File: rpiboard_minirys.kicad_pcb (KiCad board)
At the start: 4 copper layers, 65 x 56 mm, 128 parts, among them IC1 LM51231QRGRRQ1, IC2 TPS564242DRLR, IC3 L6470H, IC4 L6470H, IC5 74AUP2G00DC,125, IC6 MAX11613EUA+T, J1 RPi_GPIO, J10 ToF1_Sensor, J11 ToF2_Sensor, J12 ToF3_Sensor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

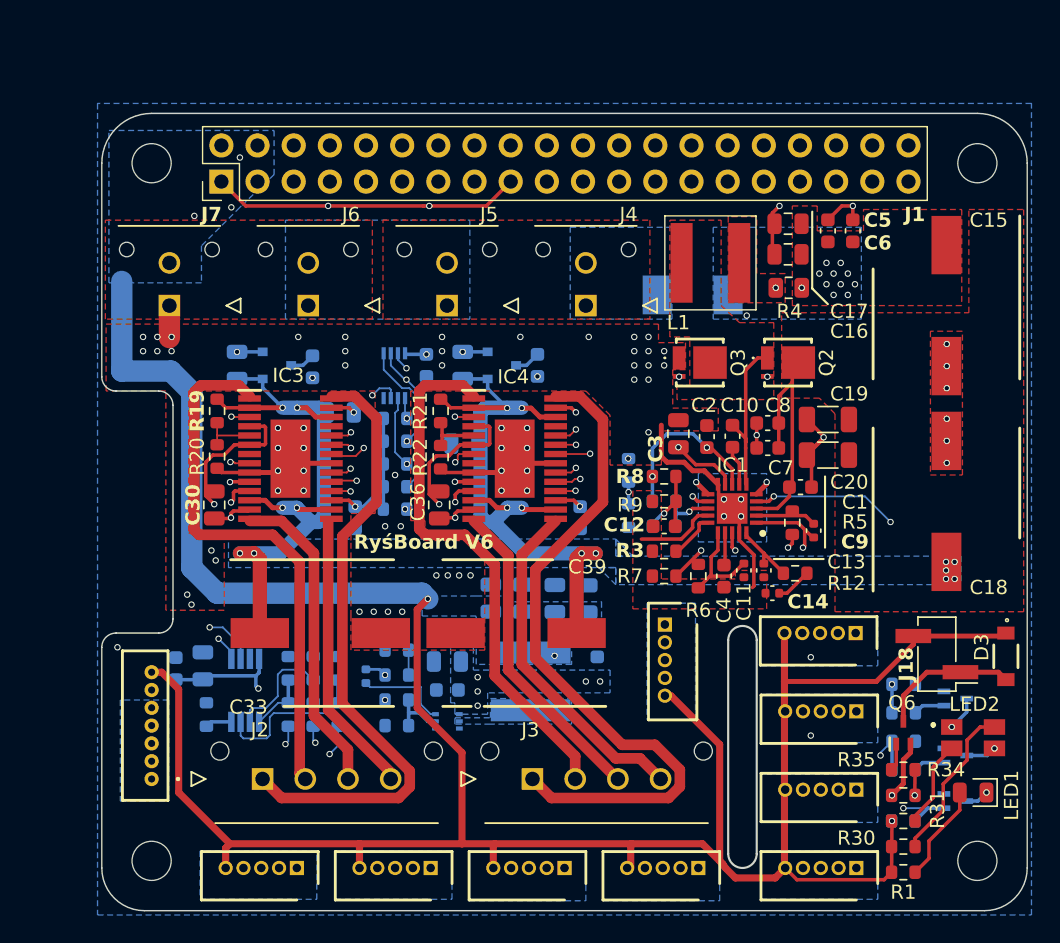
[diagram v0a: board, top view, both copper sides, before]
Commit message: Left drivers internal voltage regulator now has its own capacitors
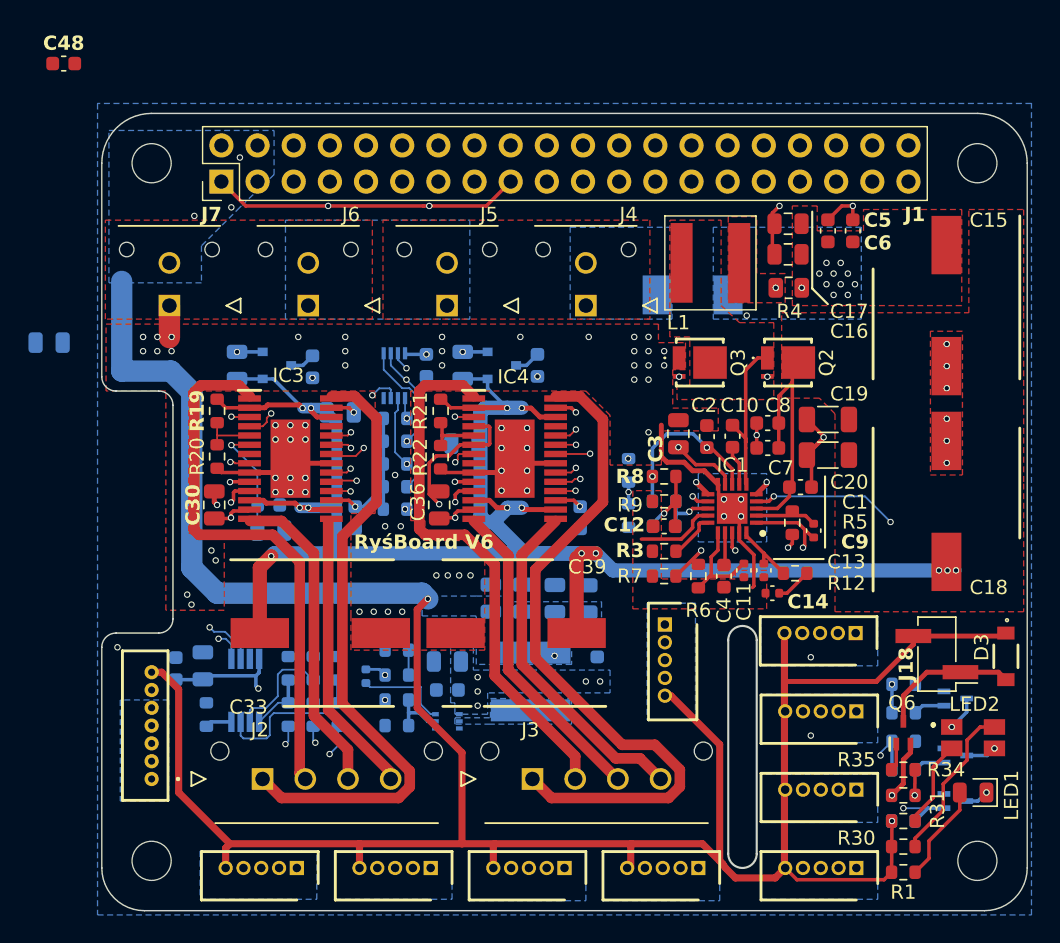
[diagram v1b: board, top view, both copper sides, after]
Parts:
- added C45: 10uF, Capacitor_SMD:C_0805_2012Metric, B.Cu at (33.4, 50.8)
- added C46: 100nF, Capacitor_SMD:C_0603_1608Metric, B.Cu at (33.2, 49.0)
- added C47: 10uF, Capacitor_SMD:C_0805_2012Metric, B.Cu at (17.8, 37.6)
- added C48: 100nF, Capacitor_SMD:C_0603_1608Metric, F.Cu at (18.8, 18.0)
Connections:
- IC3 pad 6: +3.3V -> +3V0
- IC4 pad 6: +3.3V -> +3V0
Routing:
- net +24V: track 106.3 -> 150.4 mm, vias 17 -> 14
- net +3V0: track 0.00 -> 8.04 mm, vias 0 -> 1
- net +3.3V: track 159.3 -> 156.6 mm, vias 8 -> 9
- net GND: track 72.6 -> 73.8 mm, vias 81 -> 85
- removed copper zone on B.Cu, net +24V

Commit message: Separated 3V0 and 3V3 lines, right motor driver properly connected, fixed trace pathing
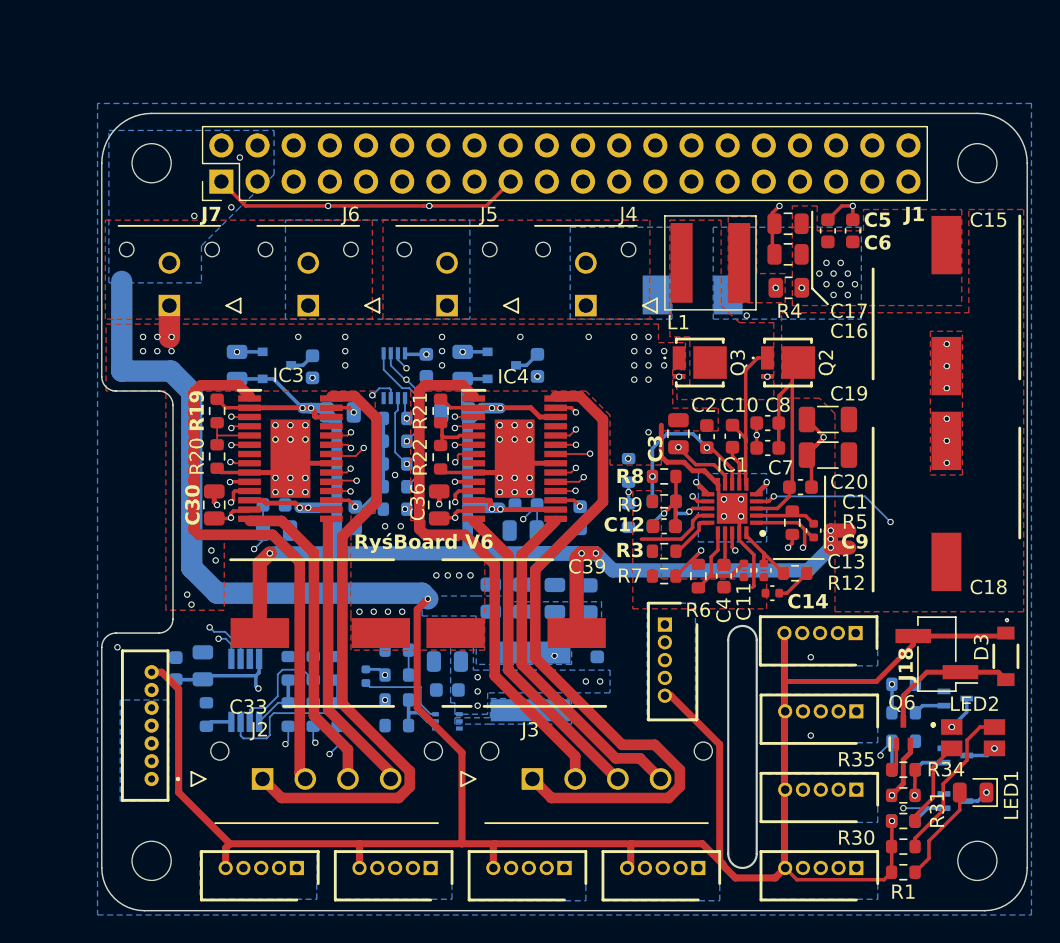
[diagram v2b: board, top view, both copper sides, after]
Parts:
- C48: moved to B.Cu
- moved C48 44.9 mm to (51.3, 49.0), turned to 180 degrees
- moved C47 35.8 mm to (51.1, 50.8)
- moved C40 2.31 mm to (46.3, 42.5)
- moved C45 0.40 mm to (33.8, 50.8)
- moved C46 0.38 mm to (33.6, 49.0)
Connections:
- C45 pad 1: +3V0 -> /Motor_Controllers/3V_VREG_ML
- C46 pad 1: +3V0 -> /Motor_Controllers/3V_VREG_ML
- C47 pad 1: +3V0 -> /Motor_Controllers/3V_VREG_MR
- C48 pad 1: +3V0 -> /Motor_Controllers/3V_VREG_MR
- IC3 pad 6: +3V0 -> /Motor_Controllers/3V_VREG_ML
- IC4 pad 6: +3V0 -> /Motor_Controllers/3V_VREG_MR
- R23 pad 1: +3.3V -> GND
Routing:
- net /Motor_Controllers/3V_VREG_MR: track 0.00 -> 15.1 mm, vias 0 -> 2
- net /Motor_Controllers/3V_VREG_ML: track 0.00 -> 12.6 mm, vias 0 -> 2
- net +3V0: track 8.04 -> 0.00 mm, vias 1 -> 0
- net +3.3V: track 156.6 -> 153.3 mm, vias 9 -> 10
- net +24V: track 150.4 -> 147.3 mm
- net /Motor_Controllers/SPI_BRIDGE: track 24.8 -> 23.1 mm
- net /Connectors/SPI_CLK: track 83.4 -> 84.8 mm
- net /Connectors/~{M_STBY}: track 44.6 -> 45.3 mm
- net GND: vias 85 -> 89

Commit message: Added proper silkscreen info for connectors
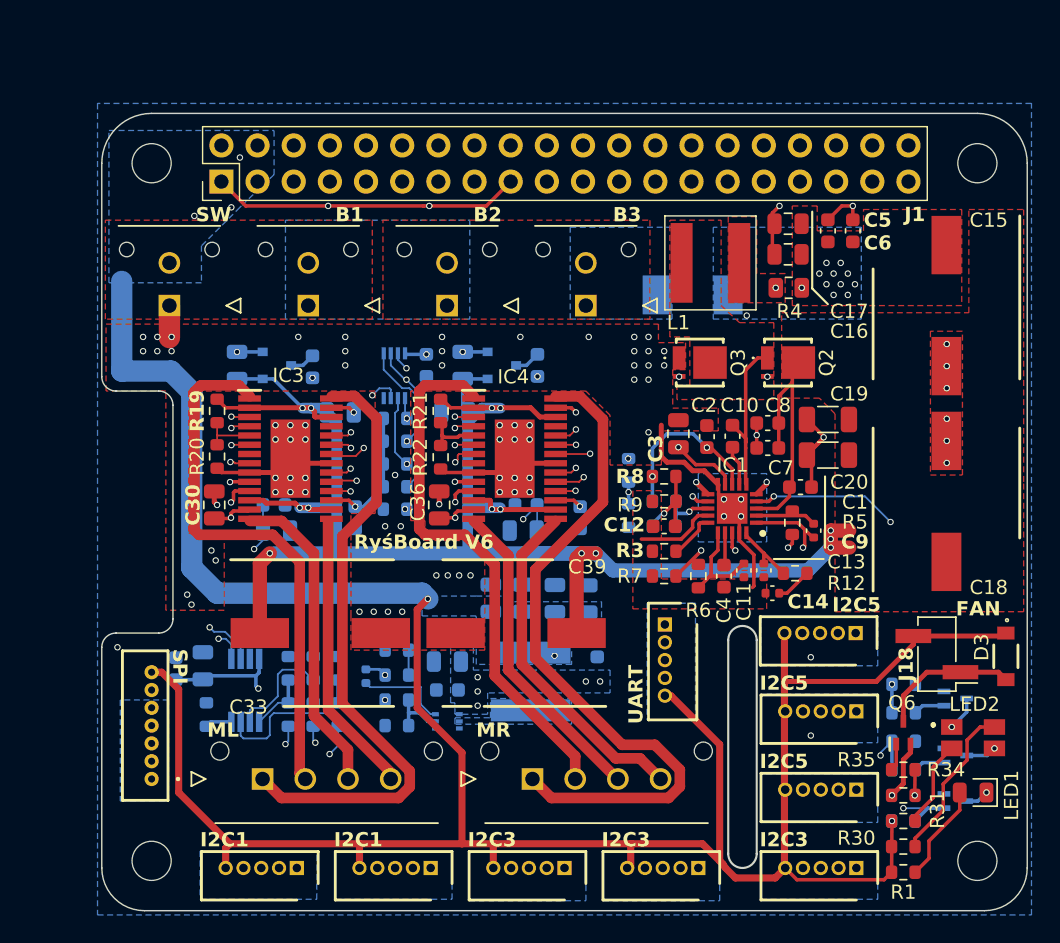
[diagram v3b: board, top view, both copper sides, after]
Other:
- board text added: "B1"
- board text added: "B2"
- board text added: "B3"
- board text added: "FAN"
- board text added: "I2C1"
- board text added: "I2C3"
- board text added: "I2C5"
- board text added: "ML"
- board text added: "MR"
- board text added: "SPI"
- board text added: "SW"
- board text added: "UART"
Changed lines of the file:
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@@
     (property "ki_keywords" "connector")
     (attr through_hole)
-    (fp_text reference "J4" (at 3 -6.4) (layer "F.SilkS")
-        (effects (font (size 1 1) (thickness 0.2)))
+    (fp_text reference "J4" (at 2 0.1) (layer "B.SilkS")
+        (effects (font (size 1 1) (thickness 0.2)) (justify mirror))
     )
     (fp_text value "B_Cell_3" (at 0 0) (layer "F.SilkS") hide
@@
     (property "ki_keywords" "connector")
     (attr through_hole)
-    (fp_text reference "J3" (at 0.15 3.45) (layer "F.SilkS")
-        (effects (font (size 1 1) (thickness 0.2)))
+    (fp_text reference "J3" (at -0.05 -2.05) (layer "B.SilkS")
+        (effects (font (size 1 1) (thickness 0.2)) (justify mirror))
     )
     (fp_text value "Motor_R" (at 0 0) (layer "F.SilkS") hide
@@
     (property "ki_keywords" "connector")
     (attr through_hole)
-    (fp_text reference "J6" (at 3 -6.4) (layer "F.SilkS")
-        (effects (font (size 1 1) (thickness 0.2)))
+    (fp_text reference "J6" (at 2 0.1) (layer "B.SilkS")
+        (effects (font (size 1 1) (thickness 0.2)) (justify mirror))
     )
     (fp_text value "B_Cell_1" (at 0 0) (layer "F.SilkS") hide
@@
     (property "ki_keywords" "connector")
     (attr through_hole)
-    (fp_text reference "J5" (at 2.95 -6.4) (layer "F.SilkS")
-        (effects (font (size 1 1) (thickness 0.2)))
+    (fp_text reference "J5" (at 1.95 0.1) (layer "B.SilkS")
+        (effects (font (size 1 1) (thickness 0.2)) (justify mirror))
     )
     (fp_text value "B_Cell_2" (at 0 0) (layer "F.SilkS") hide
@@
     (property "ki_keywords" "connector")
     (attr through_hole)
-    (fp_text reference "J7" (at 2.95 -6.4) (layer "F.SilkS")
-        (effects (font (size 1 1) (thickness 0.2) bold))
+    (fp_text reference "J7" (at 1.95 0.1) (layer "B.SilkS")
+        (effects (font (size 1 1) (thickness 0.2) bold) (justify mirror))
     )
     (fp_text value "SW" (at 0 0) (layer "F.SilkS") hide
@@
     (property "ki_keywords" "connector")
     (attr through_hole)
-    (fp_text reference "J2" (at 0.19215 3.45) (layer "F.SilkS")
-        (effects (font (size 1 1) (thickness 0.2)))
+    (fp_text reference "J2" (at -0.00785 -2.05) (layer "B.SilkS")
+        (effects (font (size 1 1) (thickness 0.2)) (justify mirror))
     )
     (fp_text value "Motor_L" (at 0 0) (layer "F.SilkS") hide
@@
     (effects (font (size 1 1) (thickness 0.2) bold) (justify left bottom mirror))
   )
+  (gr_text "I2C5" (at 67.7 62.1) (layer "F.SilkS")
+    (effects (font (size 1 1) (thickness 0.2) bold) (justify left bottom))
+  )
+  (gr_text "ML" (at 28.9 65.4) (layer "F.SilkS")
+    (effects (font (size 1 1) (thickness 0.2) bold) (justify left bottom))
+  )
+  (gr_text "I2C3" (at 47.2 73.1) (layer "F.SilkS")
+    (effects (font (size 1 1) (thickness 0.2) bold) (justify left bottom))
+  )
+  (gr_text "I2C1" (at 28.4 73.1) (layer "F.SilkS")
+    (effects (font (size 1 1) (thickness 0.2) bold) (justify left bottom))
+  )
+  (gr_text "FAN" (at 81.485 56.88) (layer "F.SilkS")
+    (effects (font (size 1 1) (thickness 0.2) bold) (justify left bottom))
+  )
+  (gr_text "UART" (at 59.6 64.4 90) (layer "F.SilkS")
+    (effects (font (size 1 1) (thickness 0.2) bold) (justify left bottom))
+  )
+  (gr_text "I2C3" (at 67.7 73.1) (layer "F.SilkS")
+    (effects (font (size 1 1) (thickness 0.2) bold) (justify left bottom))
+  )
+  (gr_text "B2" (at 47.6 29.2) (layer "F.SilkS")
+    (effects (font (size 1 1) (thickness 0.2) bold) (justify left bottom))
+  )
+  (gr_text "MR" (at 47.8 65.4) (layer "F.SilkS")
+    (effects (font (size 1 1) (thickness 0.2) bold) (justify left bottom))
+  )
+  (gr_text "B1" (at 37.9 29.2) (layer "F.SilkS")
+    (effects (font (size 1 1) (thickness 0.2) bold) (justify left bottom))
+  )
+  (gr_text "SPI\n" (at 26.4 59.1 270) (layer "F.SilkS")
+    (effects (font (size 1 1) (thickness 0.2) bold) (justify left bottom))
+  )
+  (gr_text "I2C5" (at 72.8 56.6) (layer "F.SilkS")
+    (effects (font (size 1 1) (thickness 0.2) bold) (justify left bottom))
+  )
+  (gr_text "I2C1" (at 37.8 73.1) (layer "F.SilkS")
+    (effects (font (size 1 1) (thickness 0.2) bold) (justify left bottom))
+  )
+  (gr_text "B3" (at 57.4 29.2) (layer "F.SilkS")
+    (effects (font (size 1 1) (thickness 0.2) bold) (justify left bottom))
+  )
+  (gr_text "SW" (at 28.1 29.2) (layer "F.SilkS")
+    (effects (font (size 1 1) (thickness 0.2) bold) (justify left bottom))
+  )
+  (gr_text "I2C3" (at 56.6 73.1) (layer "F.SilkS")
+    (effects (font (size 1 1) (thickness 0.2) bold) (justify left bottom))
+  )
   (gr_text "RyśBoard V6" (at 39.2 52.2) (layer "F.SilkS")
     (effects (font (size 1 1) (thickness 0.2) bold) (justify left bottom))
   )
+  (gr_text "I2C5" (at 67.7 67.6) (layer "F.SilkS")
+    (effects (font (size 1 1) (thickness 0.2) bold) (justify left bottom))
+  )

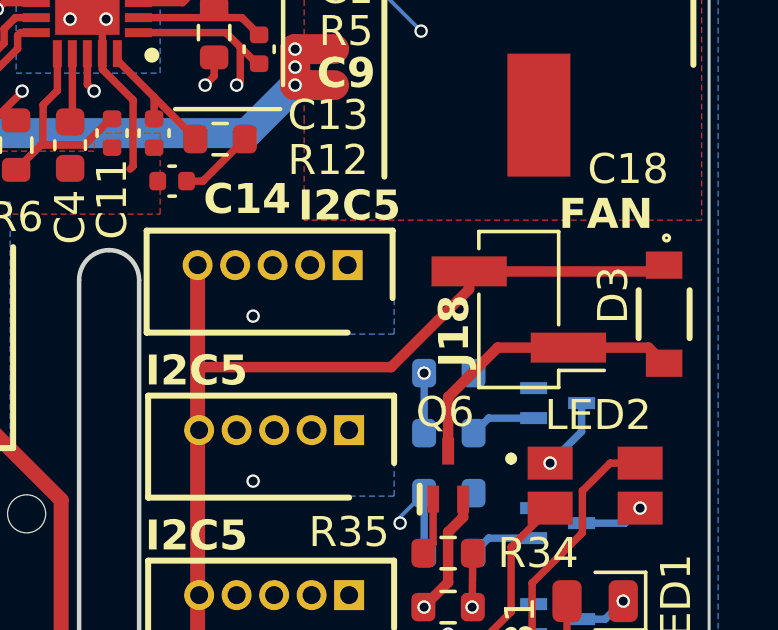
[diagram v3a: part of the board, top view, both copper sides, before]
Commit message: Changed fan connector type to THT
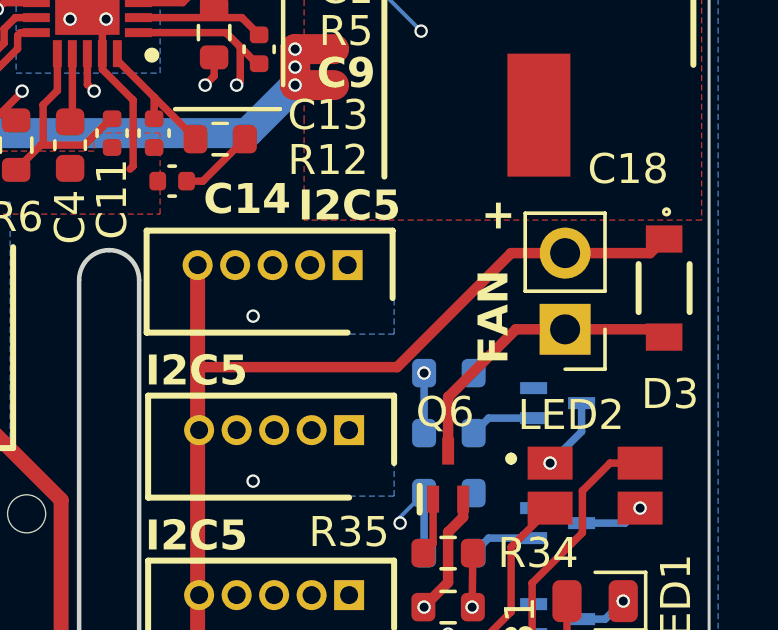
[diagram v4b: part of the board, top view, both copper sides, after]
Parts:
- J18: footprint Connector_PinHeader_2.54mm:PinHeader_1x02_P2.54mm_Vertical_SMD_Pin1Left -> Connector_PinHeader_2.54mm:PinHeader_1x02_P2.54mm_Vertical
- moved J18 1.68 mm to (81.7, 60.1)
- moved D3 0.87 mm to (85.0, 58.8)
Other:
- board text added: "+"

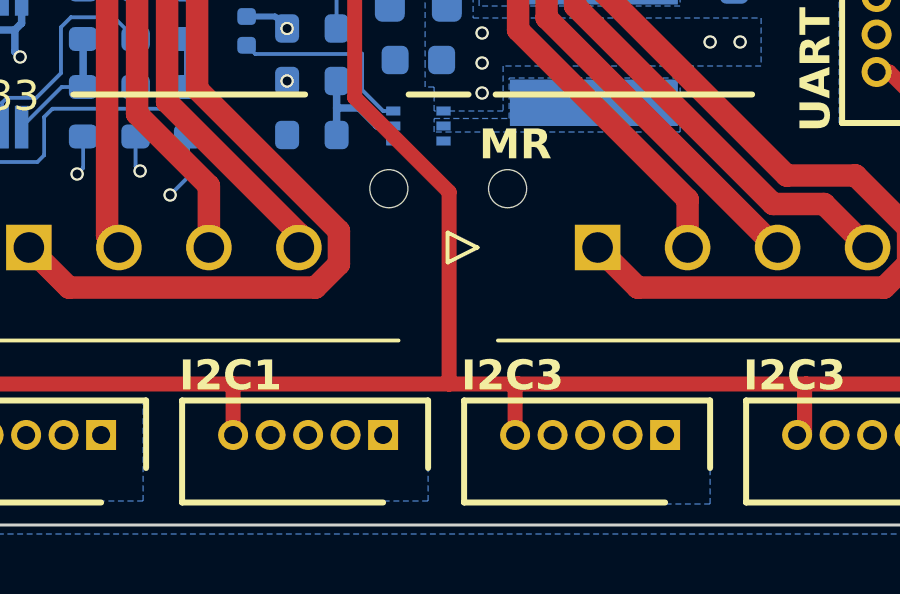
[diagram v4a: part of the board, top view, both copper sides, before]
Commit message: Added useful markings on silkscreen
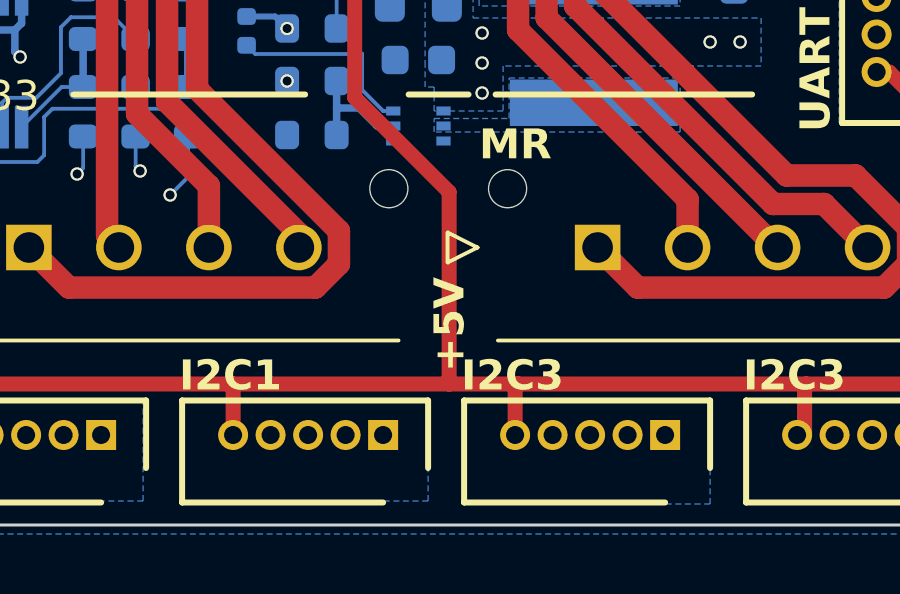
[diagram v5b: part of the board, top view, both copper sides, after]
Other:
- board text added: "+24V"
- board text added: "+5V"
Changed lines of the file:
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@@
+    (effects (font (size 1 1) (thickness 0.2) bold) (justify left bottom mirror))
+  )
+  (gr_text "+" (at 55.5 31) (layer "B.SilkS")
+    (effects (font (size 1 1) (thickness 0.2) bold) (justify left bottom mirror))
+  )
+  (gr_text "+24V" (at 70.8 54.2) (layer "B.SilkS")
+    (effects (font (size 1 1) (thickness 0.2) bold) (justify left bottom mirror))
+  )
+  (gr_text "+" (at 36 31) (layer "B.SilkS")
+    (effects (font (size 1 1) (thickness 0.2) bold) (justify left bottom mirror))
+  )
+  (gr_text "+" (at 45.7 31) (layer "B.SilkS")
     (effects (font (size 1 1) (thickness 0.2) bold) (justify left bottom mirror))
   )
@@
     (effects (font (size 1 1) (thickness 0.2) bold) (justify left bottom))
   )
+  (gr_text "+5V" (at 47.4 72.4 90) (layer "F.SilkS")
+    (effects (font (size 1 1) (thickness 0.2) bold) (justify left bottom))
+  )
